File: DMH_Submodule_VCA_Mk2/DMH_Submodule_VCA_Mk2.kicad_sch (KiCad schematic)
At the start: 35 parts, among them J1 Conn_01x02, J2 Conn_01x04, Q1 BC548, Q2 BC548, U1 TL072, U2 TL072

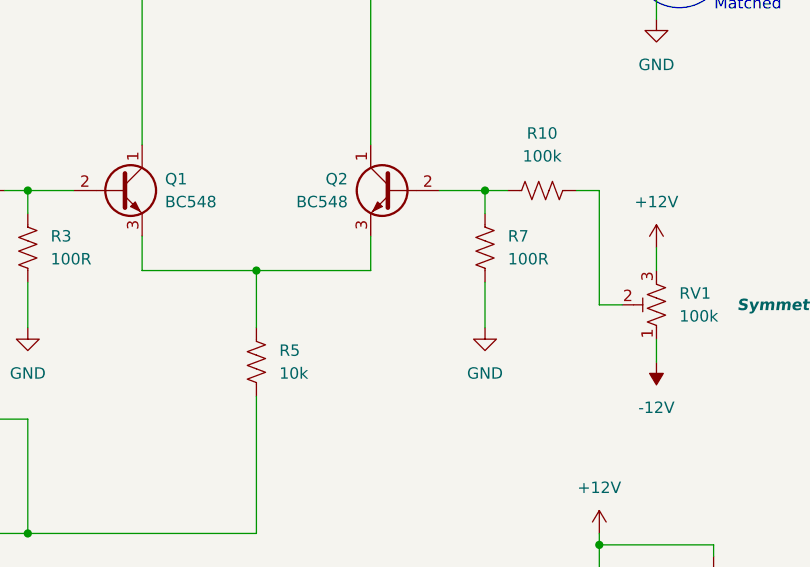
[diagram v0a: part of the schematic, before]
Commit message: Routed VCA submodule Mk2 PCB
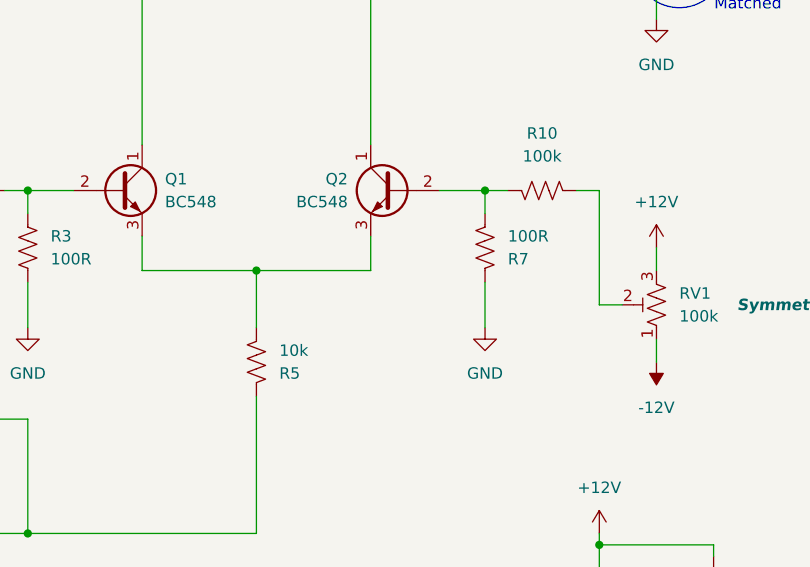
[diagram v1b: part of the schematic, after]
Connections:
- net GND: now also R7.2; no longer R7.1
- net at R1.2, U1.1: now also R5.2; no longer R5.1
- net at Q1.3 (E), Q2.3 (E): now also R5.1; no longer R5.2
- net at R10.1: now also Q2.2 (B), R7.1; no longer RV1.2
- new net: R10.2, RV1.2
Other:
- moved on the sheet: R10, R5, R7
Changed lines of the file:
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@@
 		)
 	)
-	(label "Signal_Out"
-		(at 241.3 50.8 0)
+	(label "CV In 2"
+		(at 27.94 73.66 180)
 		(effects
 			(font
 				(size 1.27 1.27)
 			)
-			(justify left bottom)
+			(justify right bottom)
 		)
 	)
-	(label "Signal_Out"
-		(at 127 156.21 180)
+	(label "Signal_In"
+		(at 125.73 88.9 180)
 		(effects
 			(font
@@
 		)
 	)
-	(label "CV In 2"
-		(at 27.94 73.66 180)
+	(label "Signal_Out"
+		(at 127 156.21 180)
 		(effects
 			(font
@@
 	)
 	(label "Signal_In"
-		(at 125.73 88.9 180)
+		(at 127 151.13 180)
 		(effects
 			(font
@@
 	)
 	(label "CV_Mix_In"
-		(at 107.95 124.46 180)
+		(at 127 153.67 180)
 		(effects
 			(font
@@
 		)
 	)
-	(label "CV In 1"
-		(at 27.94 35.56 180)
+	(label "Signal_Out"
+		(at 241.3 50.8 0)
 		(effects
 			(font
 				(size 1.27 1.27)
 			)
-			(justify right bottom)
+			(justify left bottom)
 		)
 	)
-	(label "Signal_In"
-		(at 127 151.13 180)
+	(label "CV_Mix_In"
+		(at 107.95 124.46 180)
 		(effects
 			(font
@@
 		)
 	)
-	(label "CV_Mix_In"
-		(at 127 153.67 180)
+	(label "CV In 1"
+		(at 27.94 35.56 180)
 		(effects
 			(font
@@
 	(symbol
 		(lib_id "Device:R_US")
-		(at 165.1 107.95 180)
+		(at 165.1 107.95 0)
+		(mirror y)
 		(unit 1)
 		(body_style 1)
@@
 		(in_pos_files yes)
 		(dnp no)
-		(fields_autoplaced yes)
 		(property "Reference" "R5"
-			(at 167.64 106.6799 0)
+			(at 167.64 109.2201 0)
 			(show_name no)
 			(do_not_autoplace no)
@@
 		)
 		(property "Value" "10k"
-			(at 167.64 109.2199 0)
+			(at 167.64 106.6801 0)
 			(show_name no)
 			(do_not_autoplace no)
@@
 		)
 		(property "Footprint" "Resistor_THT:R_Axial_DIN0207_L6.3mm_D2.5mm_P2.54mm_Vertical"
-			(at 164.084 107.696 90)
+			(at 164.084 108.204 90)
 			(hide yes)
 			(show_name no)
@@
 	(symbol
 		(lib_id "Device:R_US")
-		(at 190.5 95.25 180)
+		(at 190.5 95.25 0)
+		(mirror y)
 		(unit 1)
 		(body_style 1)
@@
 		(in_pos_files yes)
 		(dnp no)
-		(fields_autoplaced yes)
 		(property "Reference" "R7"
-			(at 193.04 93.9799 0)
+			(at 193.04 96.5201 0)
 			(show_name no)
 			(do_not_autoplace no)
@@
 		)
 		(property "Value" "100R"
-			(at 193.04 96.5199 0)
+			(at 193.04 93.9801 0)
 			(show_name no)
 			(do_not_autoplace no)
@@
 		)
 		(property "Footprint" "Resistor_THT:R_Axial_DIN0207_L6.3mm_D2.5mm_P2.54mm_Vertical"
-			(at 189.484 94.996 90)
+			(at 189.484 95.504 90)
 			(hide yes)
 			(show_name no)
@@
 	(symbol
 		(lib_id "Device:R_US")
-		(at 196.85 88.9 270)
+		(at 196.85 88.9 90)
+		(mirror x)
 		(unit 1)
 		(body_style 1)
@@
 		(in_pos_files yes)
 		(dnp no)
-		(fields_autoplaced yes)
 		(property "Reference" "R10"
 			(at 196.85 82.55 90)
@@
 		)
 		(property "Footprint" "Resistor_THT:R_Axial_DIN0207_L6.3mm_D2.5mm_P2.54mm_Vertical"
-			(at 196.596 89.916 90)
+			(at 197.104 89.916 90)
 			(hide yes)
 			(show_name no)

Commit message: Modified schematic
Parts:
- added C5: 33pF, Capacitor_THT:C_Disc_D3.4mm_W2.1mm_P2.50mm, symbol Device:C
- added R20, R21: 10k, Resistor_THT:R_Axial_DIN0207_L6.3mm_D2.5mm_P2.54mm_Vertical, symbol Device:R_US
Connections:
- net Signal_Out: now also C5.2
- net at R12.2, R8.1, U1.6 (-): now also C5.1, R20.1
- net at R11.1, R9.1, U1.5 (+): now also R21.1
- net at Q2.1 (C), R6.1, R9.2: now also R20.2
- net at Q1.1 (C), R4.1, R8.2: now also R21.2
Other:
- note removed: "Matched"
- moved on the sheet: R8, R9

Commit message: Redesigned PCB
Included solder bridge jumpers to selected between inverting and non-inverting mode. Added C5 for high freq stabilization.
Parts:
- removed R20, R21: 10k, Resistor_THT:R_Axial_DIN0207_L6.3mm_D2.5mm_P2.54mm_Vertical, symbol Device:R_US
- added JP1, JP2: SolderJumper_3_Open, Jumper:SolderJumper-3_P1.3mm_Open_RoundedPad1.0x1.5mm_NumberLabels, symbol Jumper:SolderJumper_3_Open
- added TP1: TestPoint_Probe, TestPoint:TestPoint_THTPad_D1.0mm_Drill0.5mm, symbol Connector:TestPoint_Probe
- C5: now fitted
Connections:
- net Signal_Out: now also TP1.1
- net at Q1.1 (C), R4.1: now also JP1.3 (B), JP2.1 (A); no longer R8.2
- net at Q2.1 (C), R6.1: now also JP1.1 (A), JP2.3 (B); no longer R9.2
- new net: JP2.2 (C), R9.2
- new net: JP1.2 (C), R8.2
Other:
- moved on the sheet: R9
